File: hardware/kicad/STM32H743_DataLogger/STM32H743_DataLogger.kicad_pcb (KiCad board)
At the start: 4 copper layers, 160 x 100 mm, 6 parts

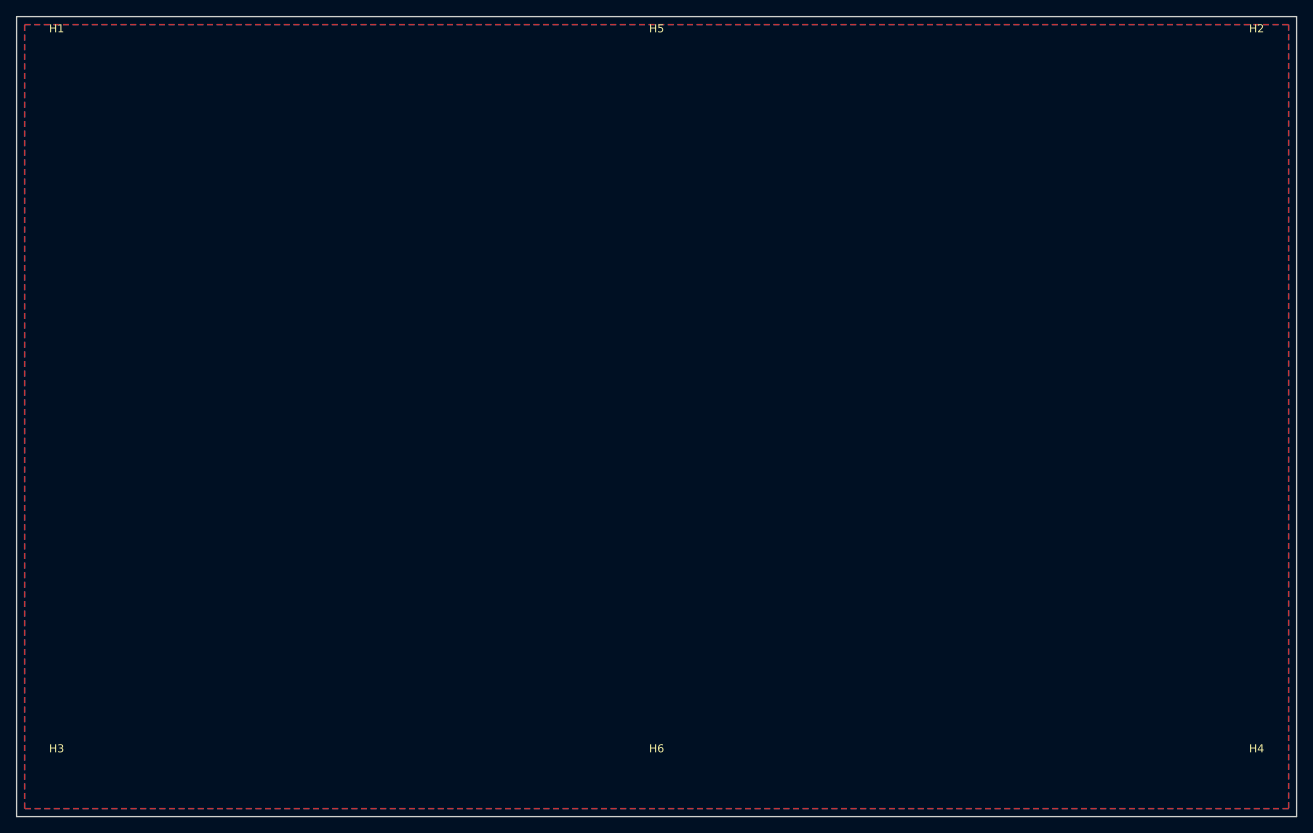
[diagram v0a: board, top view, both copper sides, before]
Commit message: feat: Add P9E silkscreen branding, fix BOM/schematic cross-check issues
- Add complete silkscreen: P9E branding (3.5mm bold), company name,
  website, product info (Weather Station v2.0), functional area labels,
  connector pin labels, LED labels, compliance marks on back
- Fix BOM: add missing J12/J13/J14/R14-R16, resolve LED4 duplicate
  (renamed to LED5 for BLE), fix C101 conflict with C104
- Complete analog input schematic channels 1-3 (TVS, precision resistors,
  anti-alias RC filter, OPA2376 U21 for Ch2-3)
- Complete digital I/O schematic: add optocouplers U32-U37, current
  limiting resistors, pull-ups R38-R44 for DI Ch1-7, relays K2-K4
- Rebrand all files from SCADA Systems to P9E Microsystems Pvt Ltd
- Update revision to 2.0, date to 2026-03-20

https://claude.ai/code/session_01XsiZ6LJT6X46LKY8yEbRbx
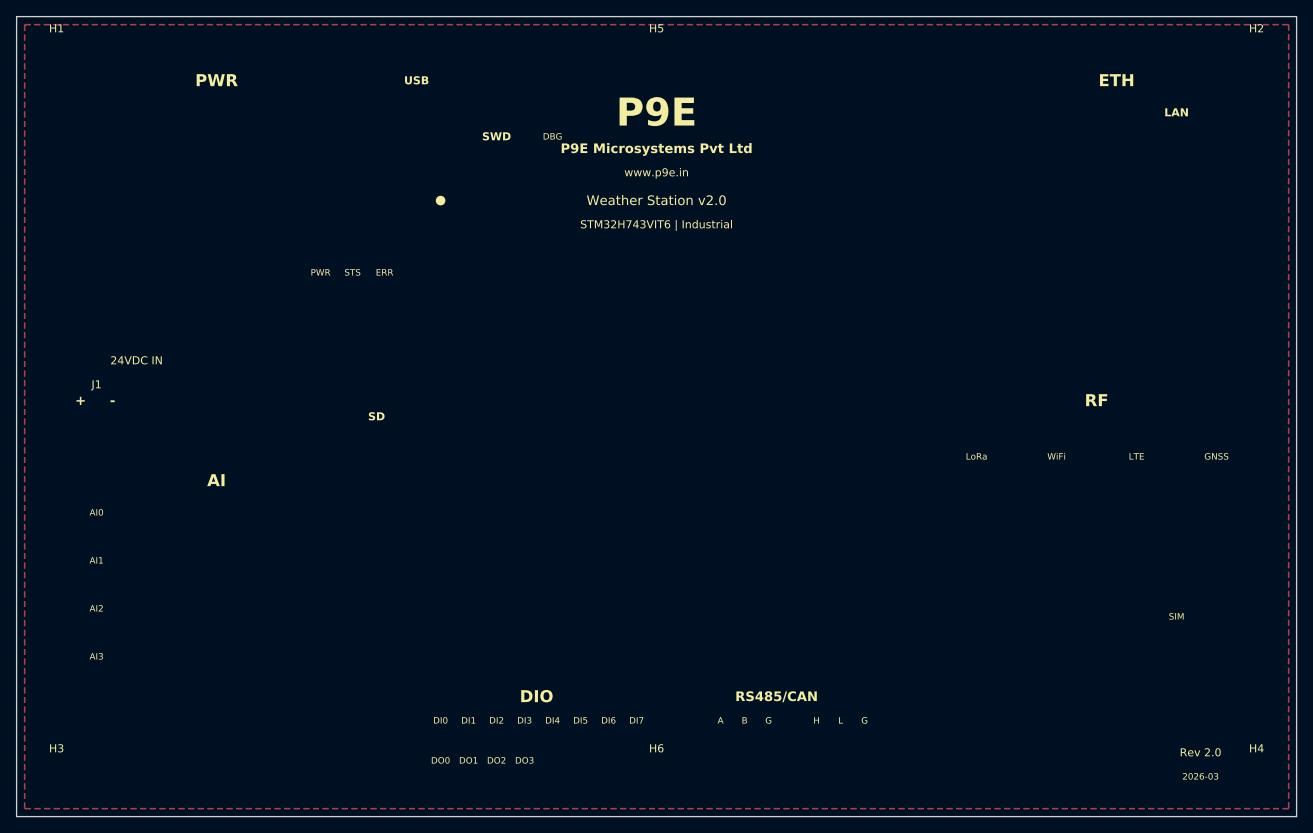
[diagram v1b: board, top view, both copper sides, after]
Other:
- board text added: "+"
- board text added: "-"
- board text added: "2026-03"
- board text added: "24VDC IN"
- board text added: "4-Layer PCB | FR-4 TG170 | ENIG | -40C to +85C"
- board text added: "A"
- board text added: "AI"
- board text added: "AI0"
- board text added: "AI1"
- board text added: "AI2"
- board text added: "AI3"
- board text added: "B"
- board text added: "CE"
- board text added: "DBG"
- board text added: "DI0"
- board text added: "DI1"
- board text added: "DI2"
- board text added: "DI3"
- board text added: "DI4"
- board text added: "DI5"
- board text added: "DI6"
- board text added: "DI7"
- board text added: "DIO"
- board text added: "DO0"
- board text added: "DO1"
- board text added: "DO2"
- board text added: "DO3"
- board text added: "ERR"
- board text added: "ETH"
- board text added: "G"
- board text added: "GNSS"
- board text added: "H"
- board text added: "J1"
- board text added: "L"
- board text added: "LAN"
- board text added: "LTE"
- board text added: "LoRa"
- board text added: "Made in India"
- board text added: "P/N: P9E-WS-200"
- board text added: "P9E"
- board text added: "P9E Microsystems Pvt Ltd"
- board text added: "PWR"
- board text added: "RF"
- board text added: "RS485/CAN"
- board text added: "Rev 2.0"
- board text added: "RoHS"
- board text added: "S/N: _______________"
- board text added: "SD"
- board text added: "SIM"
- board text added: "STM32H743VIT6 | Industrial"
- board text added: "STS"
- board text added: "SWD"
- board text added: "USB"
- board text added: "WEEE"
- board text added: "Weather Station v2.0"
- board text added: "WiFi"
- board text added: "www.p9e.in"
